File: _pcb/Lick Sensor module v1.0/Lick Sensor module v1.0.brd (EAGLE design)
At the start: 20.3 x 20.8 mm, 5 parts

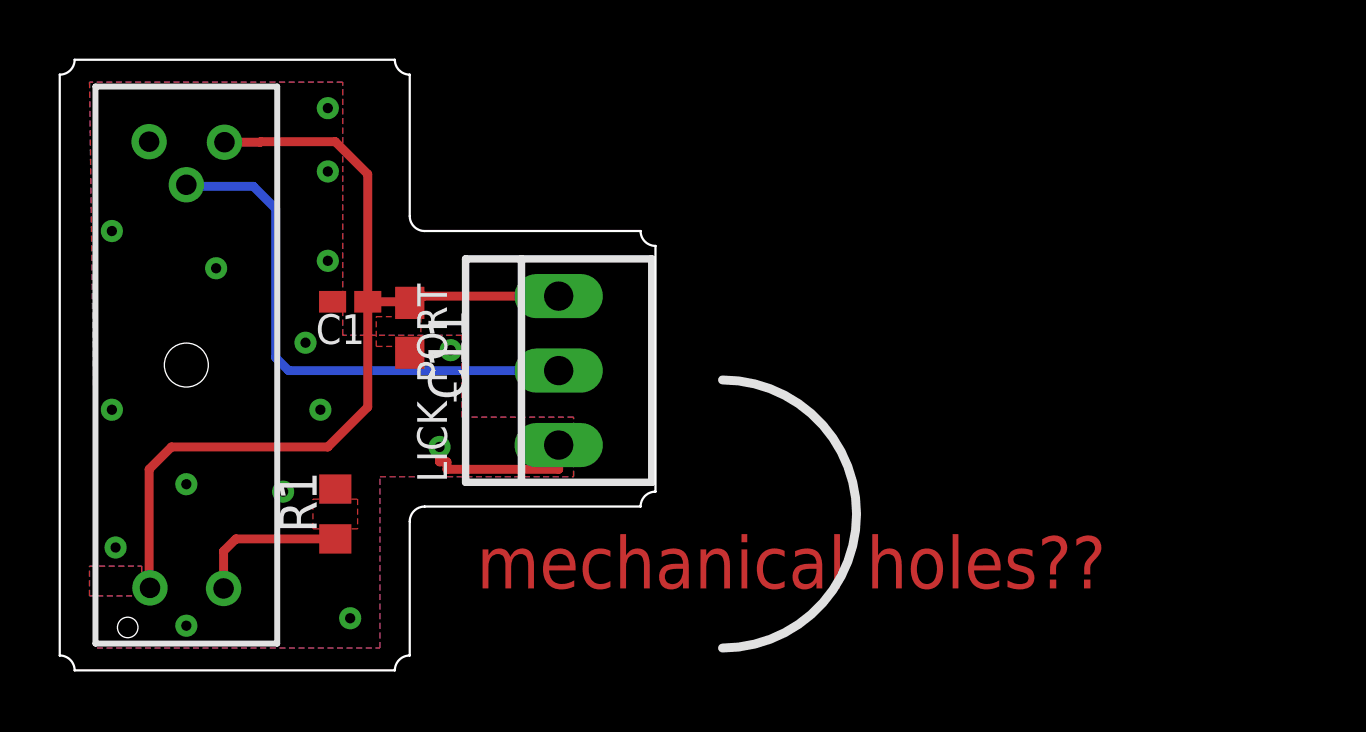
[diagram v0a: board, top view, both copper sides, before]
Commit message: update on VestibularVR & LickSensor
- returned to Eagle 9.6.2
- projects reviewed with Filipe
- LickSensor board with reviews already made
- VestibularVR  board starting implementing reviews
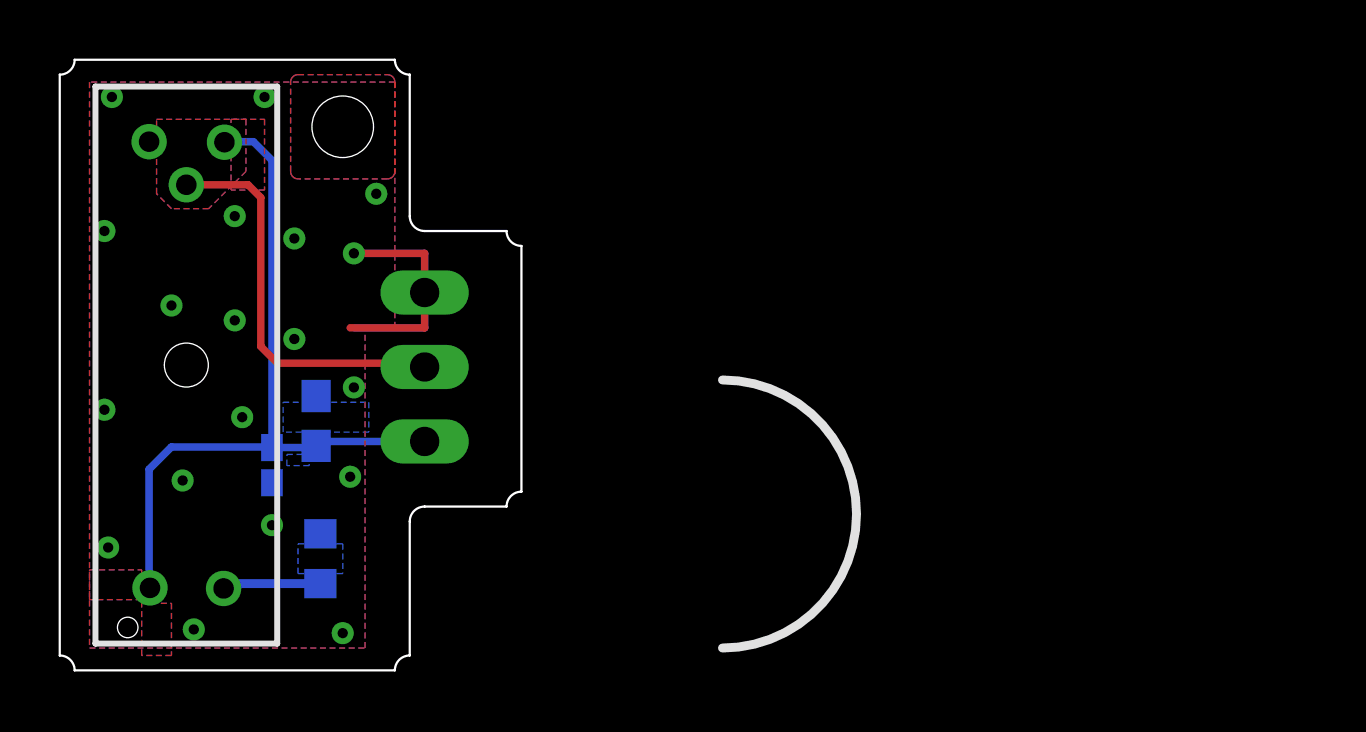
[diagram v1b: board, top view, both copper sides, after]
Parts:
- moved C1 6.18 mm to (7.24, 7.00), flipped to the bottom, turned to 270 degrees
- moved LICK_PORT 4.57 mm to (12.4, 10.3), flipped to the bottom, turned to 270 degrees
- moved C11 4.50 mm to (8.75, 8.51), flipped to the bottom, turned to 90 degrees
- moved R1 1.61 mm to (8.89, 3.81), flipped to the bottom
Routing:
- net GND: track 5.65 -> 15.0 mm, vias 15 -> 19
- net +3V3: track 33.0 -> 25.7 mm
- net N$1: track 18.3 -> 13.7 mm
- net N$2: track 5.25 -> 3.47 mm
- added copper zone on layer 1, net N$10
- added copper zone on layer 16, net N$11
- added copper zone on layer 16, net N$12
- added copper zone on layer 16, net N$13
- added copper zone on layer 16, net N$5
- added copper zone on layer 16, net N$6
- added copper zone on layer 16, net N$7
- added copper zone on layer 1, net N$8
- added copper zone on layer 1, net N$9
- added copper zone on layer 1, net X
- added copper zone on layer 16, net X1
- removed copper zone on layer 1, net N$5
- removed copper zone on layer 1, net N$6
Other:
- board size 20.3 x 20.8 mm -> 15.7 x 20.8 mm
- board text removed: "mechanical holes??"

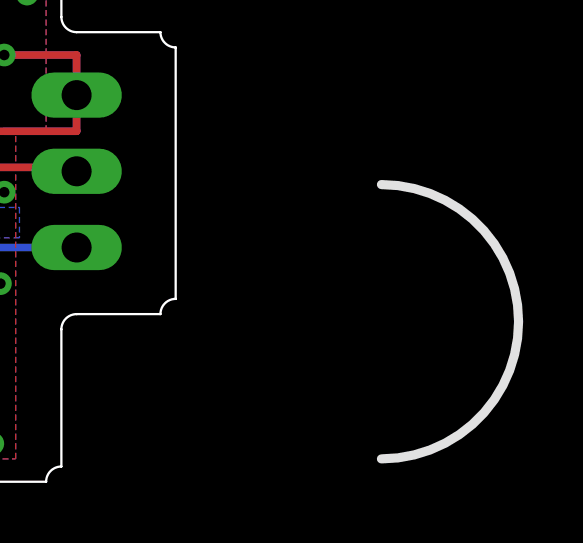
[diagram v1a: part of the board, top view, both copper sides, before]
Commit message: final versions committed & CAM data
VestibularVR H1-module v1.0
  &
Lick Sensor module v1.0
final versions committed !!!

.created CAM data for both boards
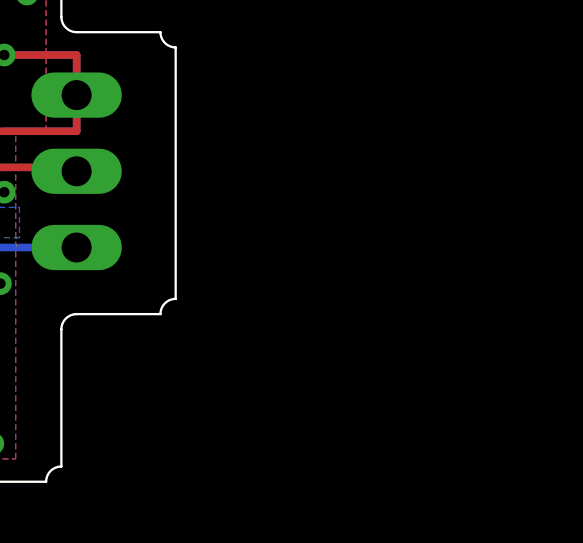
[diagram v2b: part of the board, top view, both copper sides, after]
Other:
- board text added: "3V3"
- board text added: "GND"
- board text added: "out"
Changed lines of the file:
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@@
 <layer number="23" name="tOrigins" color="15" fill="1" visible="yes" active="yes"/>
 <layer number="24" name="bOrigins" color="15" fill="1" visible="yes" active="yes"/>
-<layer number="25" name="tNames" color="7" fill="1" visible="no" active="yes"/>
+<layer number="25" name="tNames" color="7" fill="1" visible="yes" active="yes"/>
 <layer number="26" name="bNames" color="7" fill="1" visible="yes" active="yes"/>
-<layer number="27" name="tValues" color="7" fill="1" visible="no" active="yes"/>
+<layer number="27" name="tValues" color="7" fill="1" visible="yes" active="yes"/>
 <layer number="28" name="bValues" color="7" fill="1" visible="no" active="yes"/>
 <layer number="29" name="tStop" color="7" fill="3" visible="no" active="yes"/>
@@
 <wire x1="11.43" y1="20.828" x2="0.508" y2="20.828" width="0.0762" layer="20"/>
 <wire x1="0" y1="20.32" x2="0" y2="0.508" width="0.0762" layer="20"/>
-<wire x1="22.606" y1="9.906" x2="22.606" y2="0.762" width="0.3048" layer="25" curve="-180"/>
 <wire x1="0" y1="0.508" x2="0.508" y2="0" width="0.0762" layer="20" curve="-90"/>
 <wire x1="11.938" y1="5.08" x2="12.446" y2="5.588" width="0.0762" layer="20" curve="-90"/>
@@
 <wire x1="11.43" y1="0" x2="11.938" y2="0.508" width="0.0762" layer="20" curve="-90"/>
 <hole x="9.652" y="18.542" drill="2.1"/>
+<text x="5.969" y="13.462" size="1.016" layer="26" font="vector" ratio="14" distance="42" rot="MR180">GND</text>
+<text x="6.223" y="11.176" size="1.016" layer="26" font="vector" ratio="14" distance="42" rot="MR180">out</text>
+<text x="4.191" y="8.636" size="1.016" layer="26" font="vector" ratio="14" distance="42" rot="MR180">3V3</text>
 </plain>
 <attributes>
@@
 <element name="PI3" library="SparkFun" package="GP1A57HR" value="GP1A57HR" x="4.318" y="10.414" smashed="yes" rot="R90"/>
 <element name="R1" library="rcl" library_urn="urn:adsk.eagle:library:334" package="R0603" package3d_urn="urn:adsk.eagle:package:23555/2" value="1k" x="8.89" y="3.81" smashed="yes" rot="MR90">
-<attribute name="NAME" x="9.525" y="3.175" size="1.27" layer="26" rot="MR90"/>
+<attribute name="NAME" x="9.779" y="3.175" size="0.8128" layer="26" font="vector" ratio="13" rot="MR90"/>
 <attribute name="VALUE" x="6.985" y="3.175" size="1.27" layer="28" rot="MR90"/>
 </element>
@@
 <attribute name="MF" value="MOLEX" x="12.446" y="10.34855" size="1.778" layer="28" rot="MR270" display="off"/>
 <attribute name="MPN" value="22-23-2031" x="12.446" y="10.34855" size="1.778" layer="28" rot="MR270" display="off"/>
-<attribute name="NAME" x="8.636" y="14.15855" size="1.016" layer="26" ratio="10" rot="MR270"/>
+<attribute name="NAME" x="5.90745" y="15.494" size="0.8128" layer="26" font="vector" ratio="13" rot="MR180"/>
 <attribute name="OC_FARNELL" value="1462950" x="12.446" y="10.34855" size="1.778" layer="28" rot="MR270" display="off"/>
 <attribute name="OC_NEWARK" value="30C0862" x="12.446" y="10.34855" size="1.778" layer="28" rot="MR270" display="off"/>
@@
 </element>
 <element name="C1" library="rcl" library_urn="urn:adsk.eagle:library:334" package="C0402K" package3d_urn="urn:adsk.eagle:package:23679/2" value="100n" x="7.238" y="7" smashed="yes" rot="MR270">
-<attribute name="NAME" x="6.813" y="7.5" size="1.016" layer="26" rot="MR270"/>
+<attribute name="NAME" x="6.559" y="6.484" size="0.8128" layer="26" font="vector" ratio="13" rot="MR270"/>
 <attribute name="VALUE" x="8.688" y="7.5" size="1.016" layer="28" rot="MR270"/>
 </element>
 <element name="C11" library="rcl" package="C0603" value="4.7uF" x="8.746" y="8.508" smashed="yes" rot="MR90">
 <attribute name="MPN" value="C1608X6S1C475K080AC" x="8.746" y="8.508" size="1.778" layer="28" rot="MR90" display="off"/>
-<attribute name="NAME" x="9.381" y="7.873" size="1.27" layer="26" rot="MR90"/>
+<attribute name="NAME" x="9.635" y="7.619" size="0.8128" layer="26" font="vector" ratio="13" rot="MR90"/>
 <attribute name="NOTES" value="-" x="8.746" y="8.508" size="1.778" layer="28" rot="MR90" display="off"/>
 <attribute name="POPULARITY" value="73" x="8.746" y="8.508" size="1.778" layer="28" rot="MR90" display="off"/>

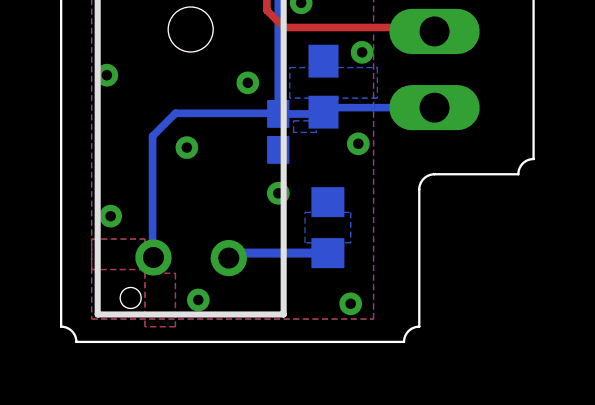
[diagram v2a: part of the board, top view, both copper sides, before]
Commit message: tunings on last versions
tunings on last versions:
  - labels size & positions
  - VestibularVR H1 module get 1mm more height
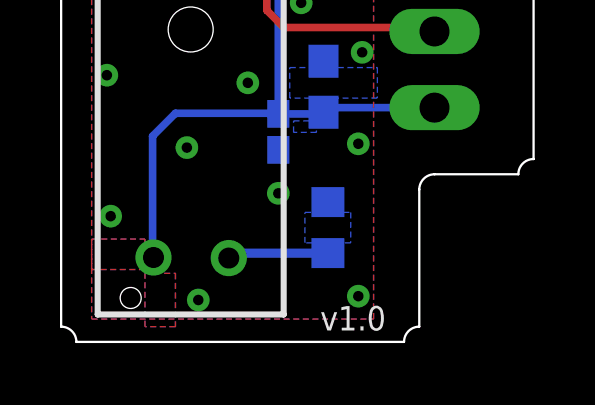
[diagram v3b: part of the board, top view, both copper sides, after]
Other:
- board text added: "OUT"
- board text added: "v1.0"
- board text removed: "out"
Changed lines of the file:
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@@
 <hole x="9.652" y="18.542" drill="2.1"/>
 <text x="5.969" y="13.462" size="1.016" layer="26" font="vector" ratio="14" distance="42" rot="MR180">GND</text>
-<text x="6.223" y="11.176" size="1.016" layer="26" font="vector" ratio="14" distance="42" rot="MR180">out</text>
-<text x="4.191" y="8.636" size="1.016" layer="26" font="vector" ratio="14" distance="42" rot="MR180">3V3</text>
+<text x="6.223" y="11.176" size="1.016" layer="26" font="vector" ratio="14" distance="42" rot="MR180">OUT</text>
+<text x="4.064" y="8.255" size="1.016" layer="26" font="vector" ratio="14" distance="42" rot="MR180">3V3</text>
+<text x="8.636" y="0.381" size="0.8128" layer="21" font="vector" ratio="15">v1.0</text>
 </plain>
 <attributes>
@@
 <attribute name="MF" value="MOLEX" x="12.446" y="10.34855" size="1.778" layer="28" rot="MR270" display="off"/>
 <attribute name="MPN" value="22-23-2031" x="12.446" y="10.34855" size="1.778" layer="28" rot="MR270" display="off"/>
-<attribute name="NAME" x="5.90745" y="15.494" size="0.8128" layer="26" font="vector" ratio="13" rot="MR180"/>
+<attribute name="NAME" x="5.90745" y="15.494" size="0.8128" layer="26" font="vector" ratio="13" rot="MR180" display="off"/>
 <attribute name="OC_FARNELL" value="1462950" x="12.446" y="10.34855" size="1.778" layer="28" rot="MR270" display="off"/>
 <attribute name="OC_NEWARK" value="30C0862" x="12.446" y="10.34855" size="1.778" layer="28" rot="MR270" display="off"/>
@@
 <via x="4.191" y="6.477" extent="1-16" drill="0.35"/>
 <via x="1.778" y="19.558" extent="1-16" drill="0.35"/>
-<via x="9.652" y="1.27" extent="1-16" drill="0.35"/>
+<via x="9.906" y="1.524" extent="1-16" drill="0.35"/>
 <contactref element="C11" pad="2"/>
 <polygon width="0.2032" layer="16">

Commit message: BOMs & start Harp Motor device H2-module v1.0
. almost final BOMs versions for VestibularVR H1-module v1.0 & Lick Sensor module v1.0
. start of new project Harp Motor device H2-module v1.0
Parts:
- LICK_PORT: value 22-23-2031 -> 1x3 case
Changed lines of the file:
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@@
 </autorouter>
 <elements>
-<element name="PI3" library="SparkFun" package="GP1A57HR" value="GP1A57HR" x="4.318" y="10.414" smashed="yes" rot="R90"/>
+<element name="PI3" library="SparkFun" package="GP1A57HR" value="GP1A57HR" x="4.318" y="10.414" smashed="yes" rot="R90">
+<attribute name="DESCRIPTION" value="SENSOR OPTICAL 10MM PCB MOUNT" x="4.318" y="10.414" size="1.778" layer="27" rot="R90" display="off"/>
+<attribute name="MPN" value="282834-3
+Digikey A98334-ND" x="4.318" y="10.414" size="1.778" layer="27" rot="R90" display="off"/>
+<attribute name="OEPS" value="OEPSK01022" x="4.318" y="10.414" size="1.778" layer="27" rot="R90" display="off"/>
+</element>
 <element name="R1" library="rcl" library_urn="urn:adsk.eagle:library:334" package="R0603" package3d_urn="urn:adsk.eagle:package:23555/2" value="1k" x="8.89" y="3.81" smashed="yes" rot="MR90">
+<attribute name="MPN" value="ERJ-2RKF1001X" x="8.89" y="3.81" size="1.778" layer="28" rot="MR90" display="off"/>
 <attribute name="NAME" x="9.779" y="3.175" size="0.8128" layer="26" font="vector" ratio="13" rot="MR90"/>
+<attribute name="OEPS" value="OEPS020006" x="8.89" y="3.81" size="1.778" layer="28" rot="MR90" display="off"/>
 <attribute name="VALUE" x="6.985" y="3.175" size="1.27" layer="28" rot="MR90"/>
 </element>
-<element name="LICK_PORT" library="con-molex" library_urn="urn:adsk.eagle:library:165" package="22-23-2031" value="22-23-2031" x="12.446" y="10.34855" smashed="yes" rot="MR270">
+<element name="LICK_PORT" library="con-molex" library_urn="urn:adsk.eagle:library:165" package="22-23-2031" value="1x3 case" x="12.446" y="10.34855" smashed="yes" rot="MR270">
 <attribute name="MF" value="MOLEX" x="12.446" y="10.34855" size="1.778" layer="28" rot="MR270" display="off"/>
-<attribute name="MPN" value="22-23-2031" x="12.446" y="10.34855" size="1.778" layer="28" rot="MR270" display="off"/>
+<attribute name="MPN" value="282834-3" x="12.446" y="10.34855" size="1.778" layer="28" rot="MR270" display="off"/>
 <attribute name="NAME" x="5.90745" y="15.494" size="0.8128" layer="26" font="vector" ratio="13" rot="MR180" display="off"/>
 <attribute name="OC_FARNELL" value="1462950" x="12.446" y="10.34855" size="1.778" layer="28" rot="MR270" display="off"/>
 <attribute name="OC_NEWARK" value="30C0862" x="12.446" y="10.34855" size="1.778" layer="28" rot="MR270" display="off"/>
+<attribute name="OEPS" value="OEPS07 xxx2   Digikey A98334-ND" x="12.446" y="10.34855" size="1.778" layer="28" rot="MR270" display="off"/>
 <attribute name="VALUE" x="17.526" y="14.15855" size="1.016" layer="28" ratio="10" rot="MR270"/>
 </element>
 <element name="C1" library="rcl" library_urn="urn:adsk.eagle:library:334" package="C0402K" package3d_urn="urn:adsk.eagle:package:23679/2" value="100n" x="7.238" y="7" smashed="yes" rot="MR270">
+<attribute name="MPN" value="GRM155R71E104KE14D" x="7.238" y="7" size="1.778" layer="28" rot="MR270" display="off"/>
 <attribute name="NAME" x="6.559" y="6.484" size="0.8128" layer="26" font="vector" ratio="13" rot="MR270"/>
+<attribute name="OEPS" value="OEPS010004" x="7.238" y="7" size="1.778" layer="28" rot="MR270" display="off"/>
 <attribute name="VALUE" x="8.688" y="7.5" size="1.016" layer="28" rot="MR270"/>
 </element>
@@
 <attribute name="MPN" value="C1608X6S1C475K080AC" x="8.746" y="8.508" size="1.778" layer="28" rot="MR90" display="off"/>
 <attribute name="NAME" x="9.635" y="7.619" size="0.8128" layer="26" font="vector" ratio="13" rot="MR90"/>
-<attribute name="NOTES" value="-" x="8.746" y="8.508" size="1.778" layer="28" rot="MR90" display="off"/>
+<attribute name="OEPS" value="OEPS010018" x="8.746" y="8.508" size="1.778" layer="28" rot="MR90" display="off"/>
 <attribute name="POPULARITY" value="73" x="8.746" y="8.508" size="1.778" layer="28" rot="MR90" display="off"/>
 <attribute name="SPICEPREFIX" value="C" x="8.746" y="8.508" size="1.778" layer="28" rot="MR90" display="off"/>
-<attribute name="TYPE" value="SMD" x="8.746" y="8.508" size="1.778" layer="28" rot="MR90" display="off"/>
 <attribute name="VALUE" x="6.841" y="7.873" size="1.27" layer="28" rot="MR90"/>
 </element>
